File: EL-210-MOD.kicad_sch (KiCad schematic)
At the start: 29 parts, among them J1 Conn_01x05, J2 Conn_01x02, P1 EL-210-KEY, U1 9-ST-20, U2 STM32G0B1KET6, U3 MAX6934AQH+D, U4 TPS613221ADBV, U5 MAX4719EUB+, U6 TLV61046ADB

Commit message: Gerber file generated
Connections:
- net at C1.2, D2.1 (K): now also D1.2 (A)
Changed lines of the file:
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@@
     (stroke (width 0) (type default) (color 0 0 0 0))
   )
-  (wire (pts (xy 129.54 171.45) (xy 129.54 176.53))
+  (wire (pts (xy 129.54 171.45) (xy 129.54 175.26))
     (stroke (width 0) (type default) (color 0 0 0 0))
   )
@@
     )
     (property "Value" "0.1u" (id 1) (at 84.201 85.5222 0)
-      (effects (font (size 1.27 1.27)) (justify left) hide)
+      (effects (font (size 1.27 1.27)) (justify left))
     )
     (property "Footprint" "Capacitor_SMD:C_0603_1608Metric_Pad1.08x0.95mm_HandSolder" (id 2) (at 82.2452 87.63 0)
@@
     (pin "5")
   )
-  (symbol (lib_name "STM32G0B1KET6_1") (lib_id "STM32G0B1KET6:STM32G0B1KET6") (at 92.71 38.1 0) (unit 1)
+  (symbol (lib_id "STM32G0B1KET6:STM32G0B1KET6") (at 92.71 38.1 0) (unit 1)
     (in_bom yes) (on_board yes)
     (property "Reference" "U2" (id 0) (at 119.38 26.67 0)

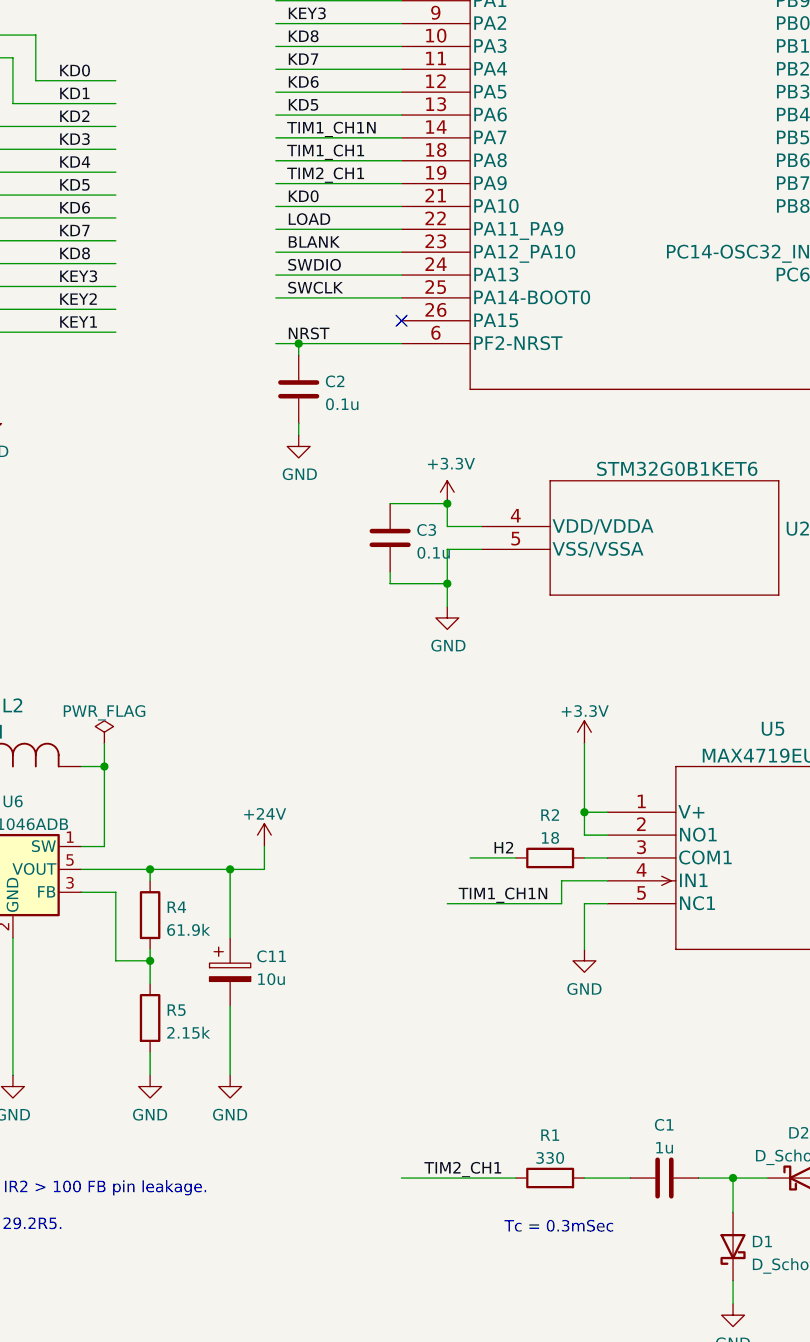
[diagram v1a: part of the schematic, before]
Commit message: Corrected signal name from TIM2_CH1 to TIM1_CH2
Fixed typo. Layout is not changed.
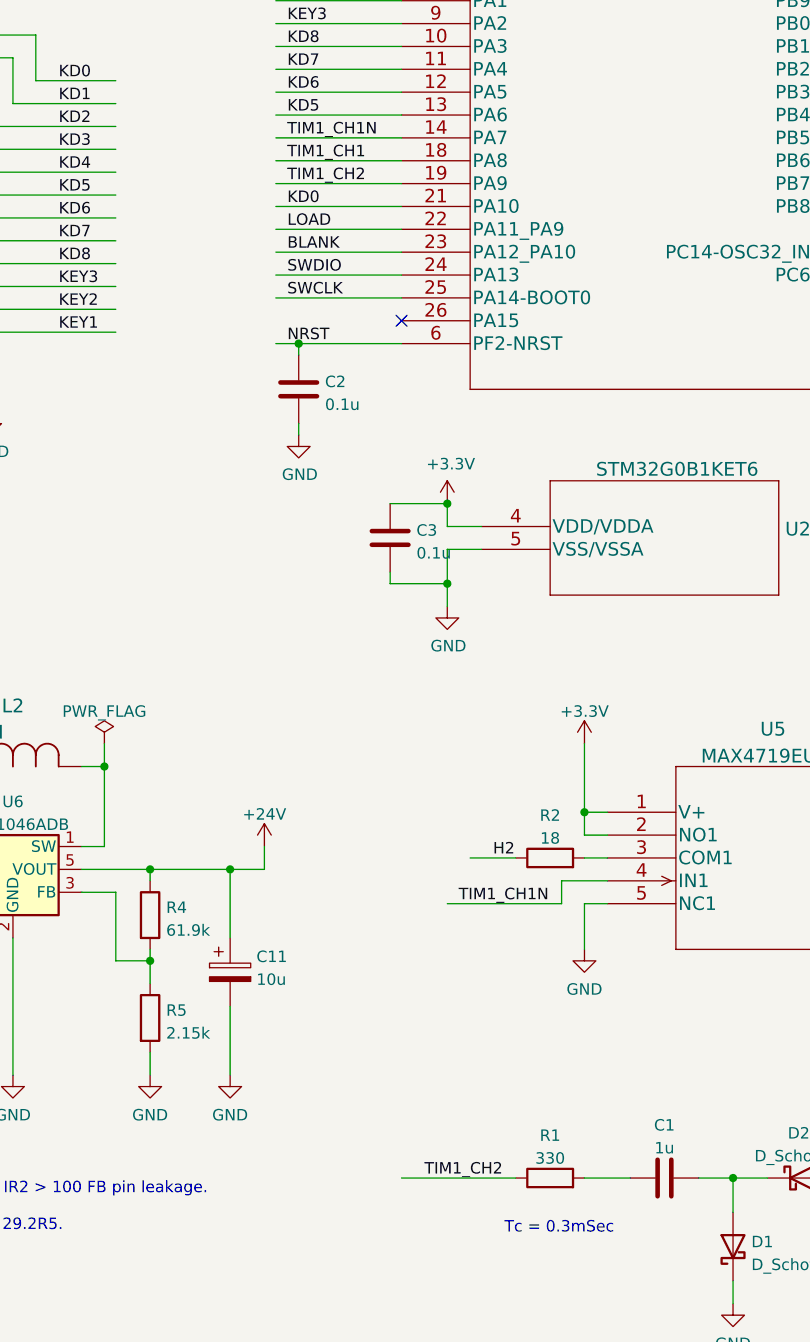
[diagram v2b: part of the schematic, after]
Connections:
- net TIM2_CH1 renamed TIM1_CH2
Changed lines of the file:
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@@
     (effects (font (size 1.27 1.27)) (justify left bottom))
   )
-  (label "TIM2_CH1" (at 80.01 60.96 0)
+  (label "TIM1_CH2" (at 80.01 60.96 0)
     (effects (font (size 1.27 1.27)) (justify left bottom))
   )
@@
     (effects (font (size 1.27 1.27)) (justify left bottom))
   )
-  (label "TIM2_CH1" (at 95.25 171.45 0)
+  (label "TIM1_CH2" (at 95.25 171.45 0)
     (effects (font (size 1.27 1.27)) (justify left bottom))
   )

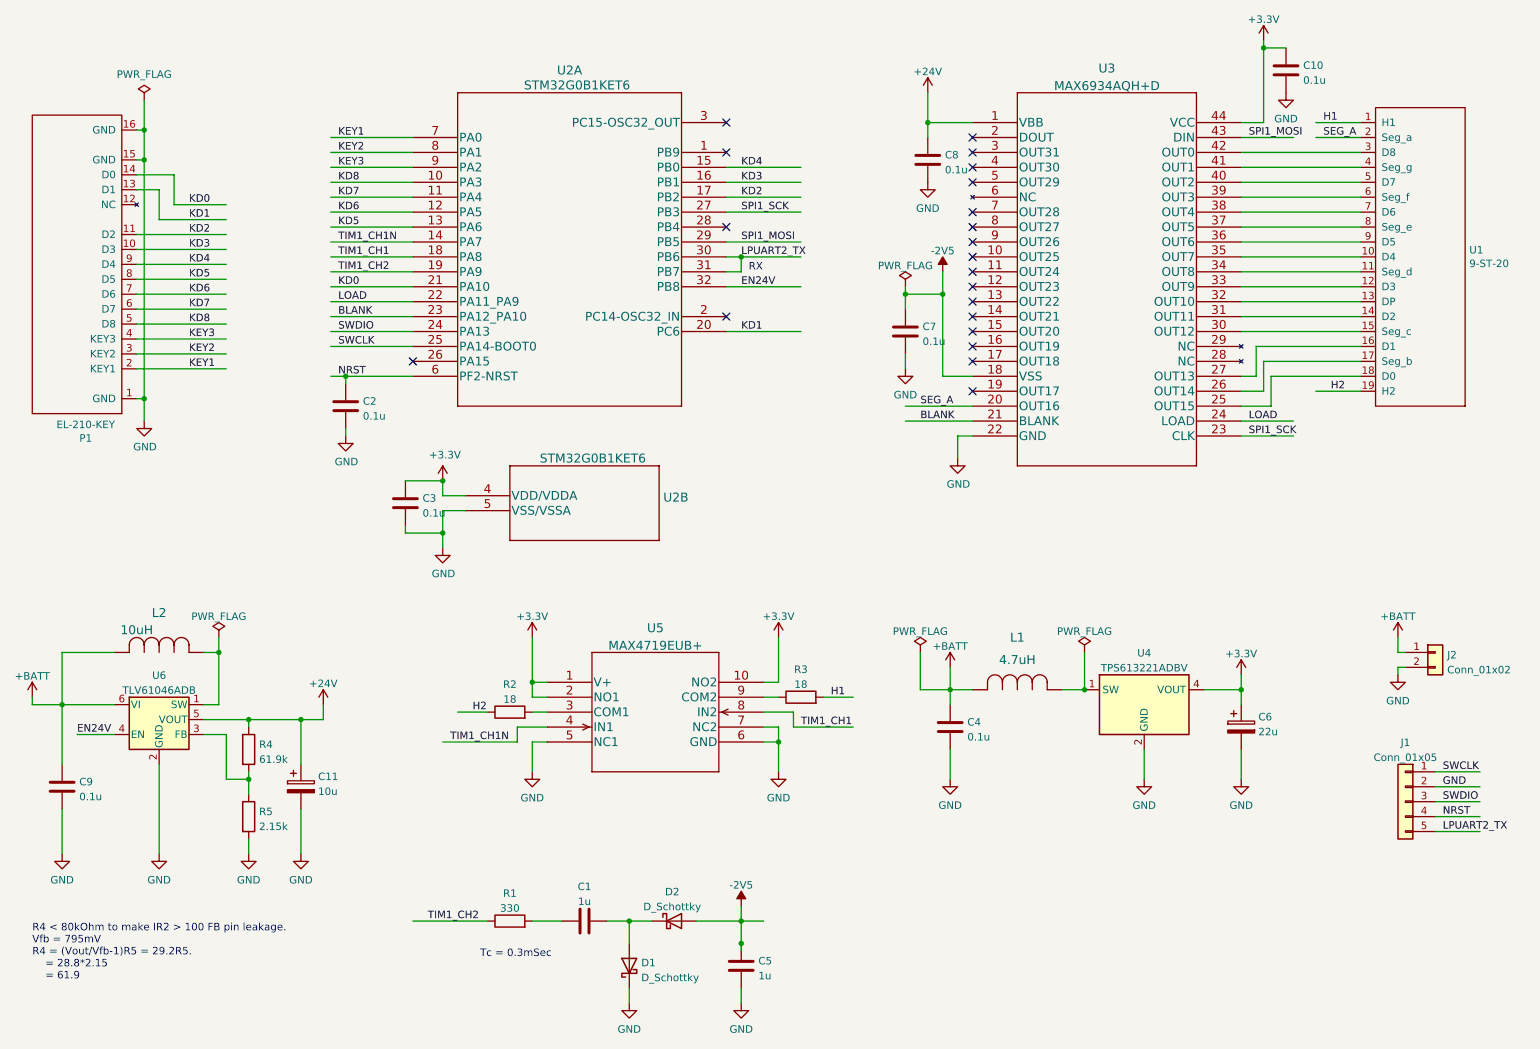
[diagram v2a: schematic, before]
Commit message: Update schematics.
- Change the key matrix signal name.
-- Including the re-order of the Key row.
- Change the value of the R1 from 330 to 18.

- Schematic is generatd in PDF.
- Layout is generated in gerber.
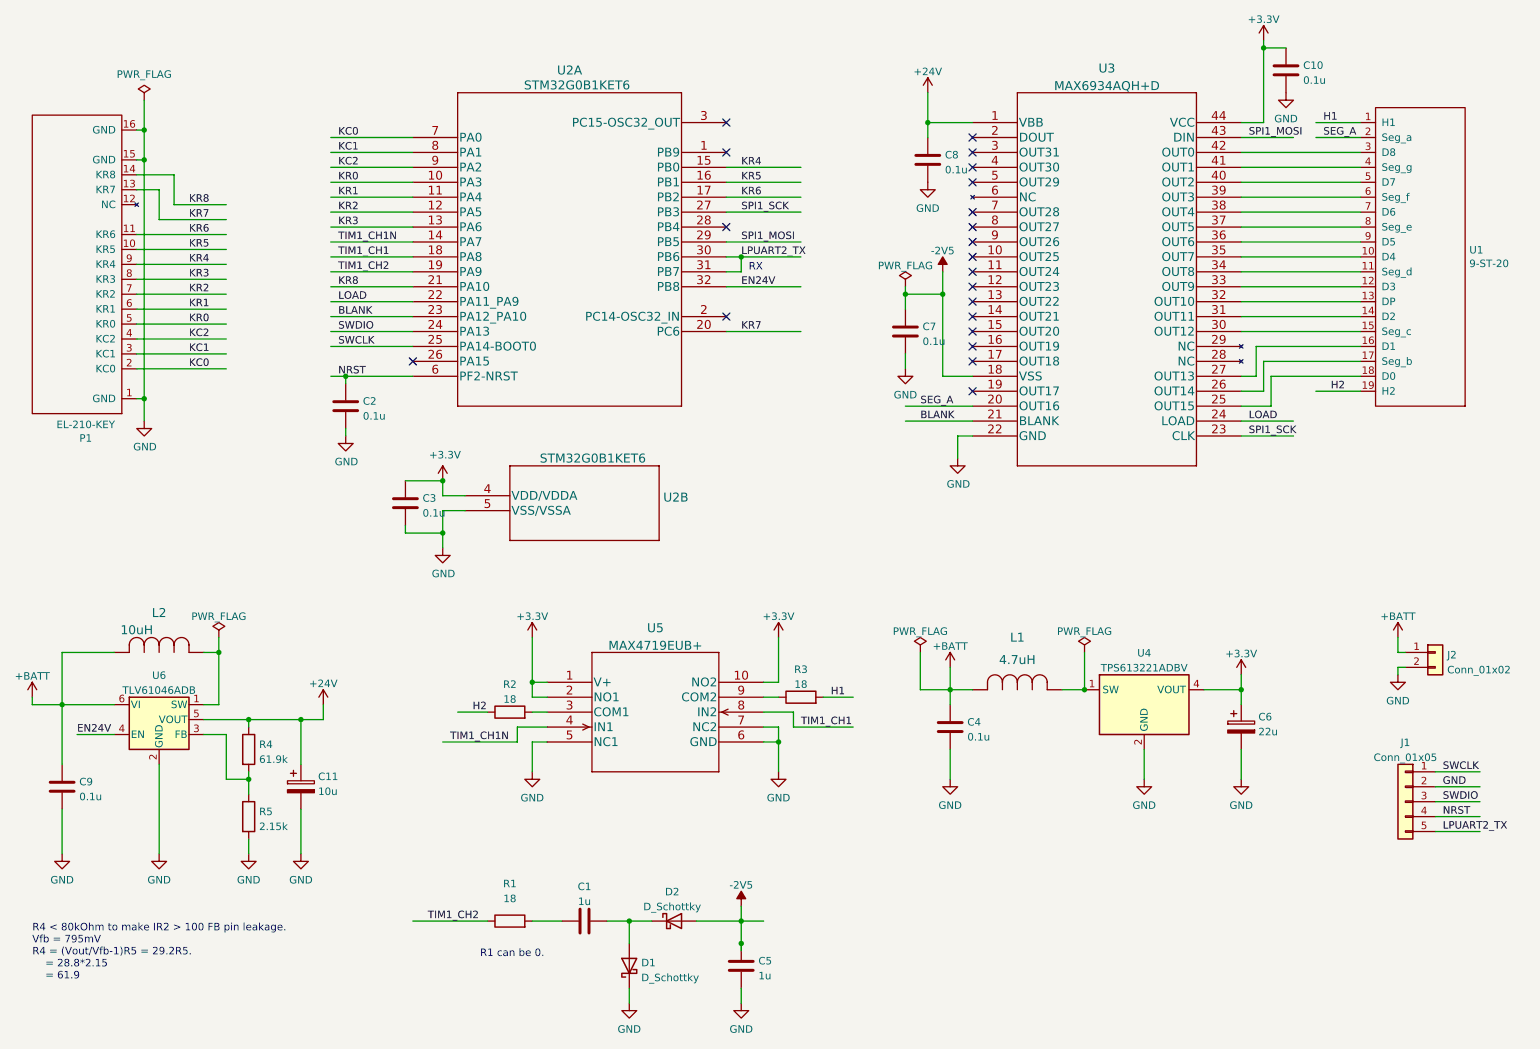
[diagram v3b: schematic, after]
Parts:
- R1: value 330 -> 18
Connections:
- net KD0 renamed KR8
- net KD1 renamed KR7
- net KD2 renamed KR6
- net KD3 renamed KR5
- net KD4 renamed KR4
- net KD5 renamed KR3
- net KD6 renamed KR2
- net KD7 renamed KR1
- net KD8 renamed KR0
- net KEY1 renamed KC0
- net KEY2 renamed KC1
- net KEY3 renamed KC2
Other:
- note added: "R1 can be 0."
- note removed: "Tc = 0.3mSec"
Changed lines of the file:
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@@
     (effects (font (size 1.27 1.27)) (justify left bottom))
   )
-  (text "Tc = 0.3mSec" (at 104.14 177.8 0)
+  (text "R1 can be 0." (at 104.14 177.8 0)
     (effects (font (size 1.27 1.27)) (justify left bottom))
   )
@@
     (effects (font (size 1.27 1.27)) (justify left bottom))
   )
-  (label "KEY2" (at 80.01 40.64 0)
-    (effects (font (size 1.27 1.27)) (justify left bottom))
-  )
-  (label "KEY1" (at 54.61 77.47 0)
+  (label "KC1" (at 80.01 40.64 0)
+    (effects (font (size 1.27 1.27)) (justify left bottom))
+  )
+  (label "KC0" (at 54.61 77.47 0)
     (effects (font (size 1.27 1.27)) (justify left bottom))
   )
@@
     (effects (font (size 1.27 1.27)) (justify left bottom))
   )
-  (label "KD7" (at 80.01 48.26 0)
+  (label "KR1" (at 80.01 48.26 0)
     (effects (font (size 1.27 1.27)) (justify left bottom))
   )
@@
     (effects (font (size 1.27 1.27)) (justify left bottom))
   )
-  (label "KD3" (at 54.61 57.15 0)
+  (label "KR5" (at 54.61 57.15 0)
     (effects (font (size 1.27 1.27)) (justify left bottom))
   )
@@
     (effects (font (size 1.27 1.27)) (justify left bottom))
   )
-  (label "KEY2" (at 54.61 74.93 0)
-    (effects (font (size 1.27 1.27)) (justify left bottom))
-  )
-  (label "KD0" (at 80.01 63.5 0)
-    (effects (font (size 1.27 1.27)) (justify left bottom))
-  )
-  (label "KD8" (at 80.01 45.72 0)
-    (effects (font (size 1.27 1.27)) (justify left bottom))
-  )
-  (label "KD8" (at 54.61 69.85 0)
+  (label "KC1" (at 54.61 74.93 0)
+    (effects (font (size 1.27 1.27)) (justify left bottom))
+  )
+  (label "KR8" (at 80.01 63.5 0)
+    (effects (font (size 1.27 1.27)) (justify left bottom))
+  )
+  (label "KR0" (at 80.01 45.72 0)
+    (effects (font (size 1.27 1.27)) (justify left bottom))
+  )
+  (label "KR0" (at 54.61 69.85 0)
     (effects (font (size 1.27 1.27)) (justify left bottom))
   )
@@
     (effects (font (size 1.27 1.27)) (justify left bottom))
   )
-  (label "KD2" (at 54.61 54.61 0)
+  (label "KR6" (at 54.61 54.61 0)
     (effects (font (size 1.27 1.27)) (justify left bottom))
   )
@@
     (effects (font (size 1.27 1.27)) (justify left bottom))
   )
-  (label "KD5" (at 80.01 53.34 0)
+  (label "KR3" (at 80.01 53.34 0)
     (effects (font (size 1.27 1.27)) (justify left bottom))
   )
@@
     (effects (font (size 1.27 1.27)) (justify left bottom))
   )
-  (label "KD4" (at 148.59 43.18 0)
+  (label "KR4" (at 148.59 43.18 0)
     (effects (font (size 1.27 1.27)) (justify left bottom))
   )
@@
     (effects (font (size 1.27 1.27)) (justify left bottom))
   )
-  (label "KD6" (at 54.61 64.77 0)
+  (label "KR2" (at 54.61 64.77 0)
     (effects (font (size 1.27 1.27)) (justify left bottom))
   )
@@
     (effects (font (size 1.27 1.27)) (justify left bottom))
   )
-  (label "KEY3" (at 80.01 43.18 0)
+  (label "KC2" (at 80.01 43.18 0)
     (effects (font (size 1.27 1.27)) (justify left bottom))
   )
@@
     (effects (font (size 1.27 1.27)) (justify left bottom))
   )
-  (label "KEY1" (at 80.01 38.1 0)
-    (effects (font (size 1.27 1.27)) (justify left bottom))
-  )
-  (label "KD6" (at 80.01 50.8 0)
+  (label "KC0" (at 80.01 38.1 0)
+    (effects (font (size 1.27 1.27)) (justify left bottom))
+  )
+  (label "KR2" (at 80.01 50.8 0)
     (effects (font (size 1.27 1.27)) (justify left bottom))
   )
@@
     (effects (font (size 1.27 1.27)) (justify left bottom))
   )
-  (label "KD5" (at 54.61 62.23 0)
+  (label "KR3" (at 54.61 62.23 0)
     (effects (font (size 1.27 1.27)) (justify left bottom))
   )
@@
     (effects (font (size 1.27 1.27)) (justify left bottom))
   )
-  (label "KD0" (at 54.61 49.53 0)
+  (label "KR8" (at 54.61 49.53 0)
     (effects (font (size 1.27 1.27)) (justify left bottom))
   )
@@
     (effects (font (size 1.27 1.27)) (justify left bottom))
   )
-  (label "KD7" (at 54.61 67.31 0)
+  (label "KR1" (at 54.61 67.31 0)
     (effects (font (size 1.27 1.27)) (justify left bottom))
   )
@@
     (effects (font (size 1.27 1.27)) (justify left bottom))
   )
-  (label "KD3" (at 148.59 45.72 0)
+  (label "KR5" (at 148.59 45.72 0)
     (effects (font (size 1.27 1.27)) (justify left bottom))
   )
@@
     (effects (font (size 1.27 1.27)) (justify left bottom))
   )
-  (label "KD2" (at 148.59 48.26 0)
+  (label "KR6" (at 148.59 48.26 0)
     (effects (font (size 1.27 1.27)) (justify left bottom))
   )
@@
     (effects (font (size 1.27 1.27)) (justify left bottom))
   )
-  (label "KD1" (at 148.59 71.12 0)
-    (effects (font (size 1.27 1.27)) (justify left bottom))
-  )
-  (label "KD1" (at 54.61 52.07 0)
-    (effects (font (size 1.27 1.27)) (justify left bottom))
-  )
-  (label "KD4" (at 54.61 59.69 0)
+  (label "KR7" (at 148.59 71.12 0)
+    (effects (font (size 1.27 1.27)) (justify left bottom))
+  )
+  (label "KR7" (at 54.61 52.07 0)
+    (effects (font (size 1.27 1.27)) (justify left bottom))
+  )
+  (label "KR4" (at 54.61 59.69 0)
     (effects (font (size 1.27 1.27)) (justify left bottom))
   )
@@
     (effects (font (size 1.27 1.27)) (justify left bottom))
   )
-  (label "KEY3" (at 54.61 72.39 0)
+  (label "KC2" (at 54.61 72.39 0)
     (effects (font (size 1.27 1.27)) (justify left bottom))
   )
@@
   (symbol (lib_id "Device:R") (at 109.22 171.45 90) (unit 1)
     (in_bom yes) (on_board yes) (fields_autoplaced)
-    (property "Reference" "R1" (id 0) (at 109.22 166.7342 90))
-    (property "Value" "330" (id 1) (at 109.22 169.2711 90))
+    (property "Reference" "R1" (id 0) (at 109.22 165.1 90))
+    (property "Value" "18" (id 1) (at 109.22 167.64 90))
     (property "Footprint" "Resistor_SMD:R_0603_1608Metric_Pad0.98x0.95mm_HandSolder" (id 2) (at 109.22 173.228 90)
       (effects (font (size 1.27 1.27)) hide)
@@
     )
     (path "/24ce6e88-9568-49e0-8e62-35eb768dc4cc"
-      (reference "R1") (unit 1) (value "330") (footprint "Resistor_SMD:R_0603_1608Metric_Pad0.98x0.95mm_HandSolder")
+      (reference "R1") (unit 1) (value "18") (footprint "Resistor_SMD:R_0603_1608Metric_Pad0.98x0.95mm_HandSolder")
     )
     (path "/7f14ad15-364d-4e44-87a6-1943a6eaf3bc"

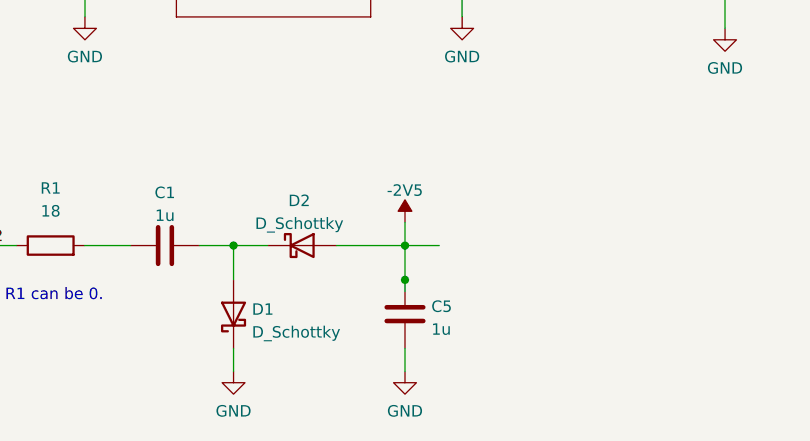
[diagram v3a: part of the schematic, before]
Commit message: Refresh the layout.
Regenerated the gerber for v1.0.1
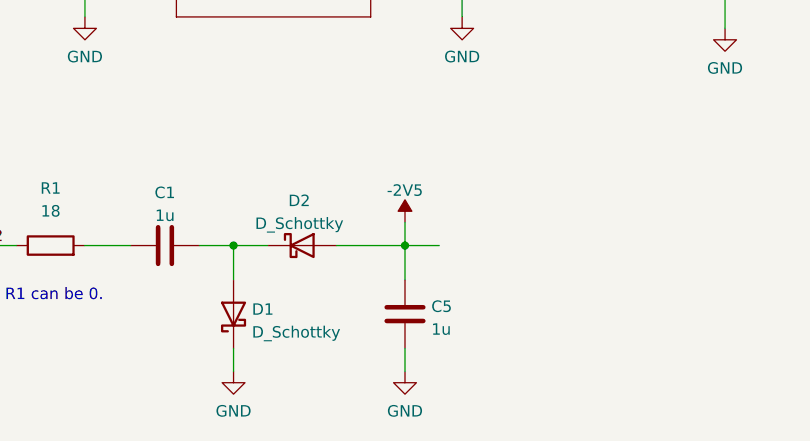
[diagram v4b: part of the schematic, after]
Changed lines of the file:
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@@
   (junction (at 182.88 64.77) (diameter 0) (color 0 0 0 0)
-  )
-  (junction (at 148.59 175.26) (diameter 0) (color 0 0 0 0)
   )
   (junction (at 46.99 82.55) (diameter 0) (color 0 0 0 0)
@@
     (stroke (width 0) (type default) (color 0 0 0 0))
   )
-  (wire (pts (xy 148.59 175.26) (xy 148.59 176.53))
-    (stroke (width 0) (type default) (color 0 0 0 0))
-  )

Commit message: Fixed foot print of the C6 and C11.
The foot prints of those capacitor was wrong.
Corrected them.
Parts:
- C11: footprint Capacitor_SMD:CP_Elec_4x3.9 -> Capacitor_SMD:CP_Elec_6.3x3.9
- C6: footprint Capacitor_SMD:CP_Elec_6.3x3.9 -> Capacitor_SMD:CP_Elec_4x3.9
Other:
- title: Akashi-10 -> EL-210-MOD
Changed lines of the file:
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@@
   (paper "A4")
   (title_block
-    (title "Akashi-10")
-    (date "2022-06-07")
-    (rev "1.0")
+    (title "EL-210-MOD")
+    (date "2023-02-12")
+    (rev "1.0.2")
   )
   (junction (at 233.68 132.08) (diameter 0) (color 0 0 0 0)
@@
       (effects (font (size 1.27 1.27)) (justify left))
     )
-    (property "Footprint" "Capacitor_SMD:CP_Elec_4x3.9" (id 2) (at 74.6252 152.4 0)
+    (property "Footprint" "Capacitor_SMD:CP_Elec_6.3x3.9" (id 2) (at 74.6252 152.4 0)
       (effects (font (size 1.27 1.27)) hide)
     )
@@
       (effects (font (size 1.27 1.27)) (justify left))
     )
-    (property "Footprint" "Capacitor_SMD:CP_Elec_6.3x3.9" (id 2) (at 234.6452 142.24 0)
+    (property "Footprint" "Capacitor_SMD:CP_Elec_4x3.9" (id 2) (at 234.6452 142.24 0)
       (effects (font (size 1.27 1.27)) hide)
     )
@@
     )
     (path "/c63c3bc3-bbbc-455a-8ec9-31c56f0d841f"
-      (reference "C6") (unit 1) (value "22u") (footprint "Capacitor_SMD:CP_Elec_6.3x3.9")
+      (reference "C6") (unit 1) (value "22u") (footprint "Capacitor_SMD:CP_Elec_4x3.9")
     )
     (path "/f5b00abc-a391-4427-9c9b-fa38c85349fd"
@@
     )
     (path "/2fdd038b-8927-431e-9c67-f8f1c25fc8d5"
-      (reference "C11") (unit 1) (value "10u") (footprint "Capacitor_SMD:CP_Elec_4x3.9")
+      (reference "C11") (unit 1) (value "10u") (footprint "Capacitor_SMD:CP_Elec_6.3x3.9")
     )
     (path "/9b4341eb-9497-42fa-9e5f-534332830100"
